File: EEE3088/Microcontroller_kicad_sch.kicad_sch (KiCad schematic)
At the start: 9 parts

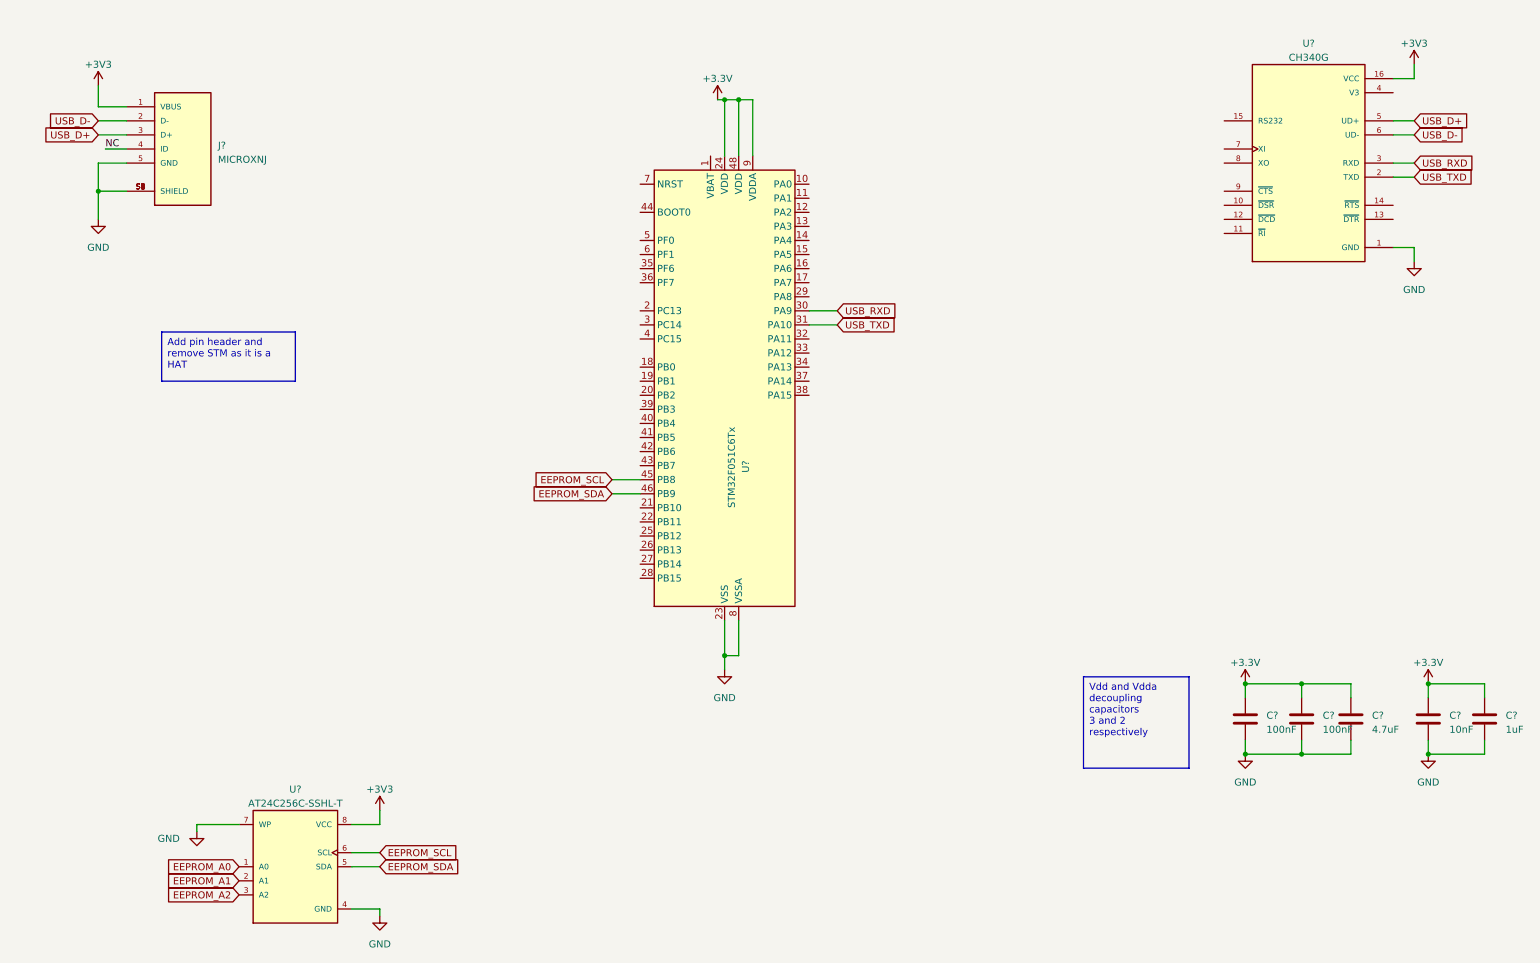
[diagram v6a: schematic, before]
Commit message: New microcontroller section
Finished and neatened up
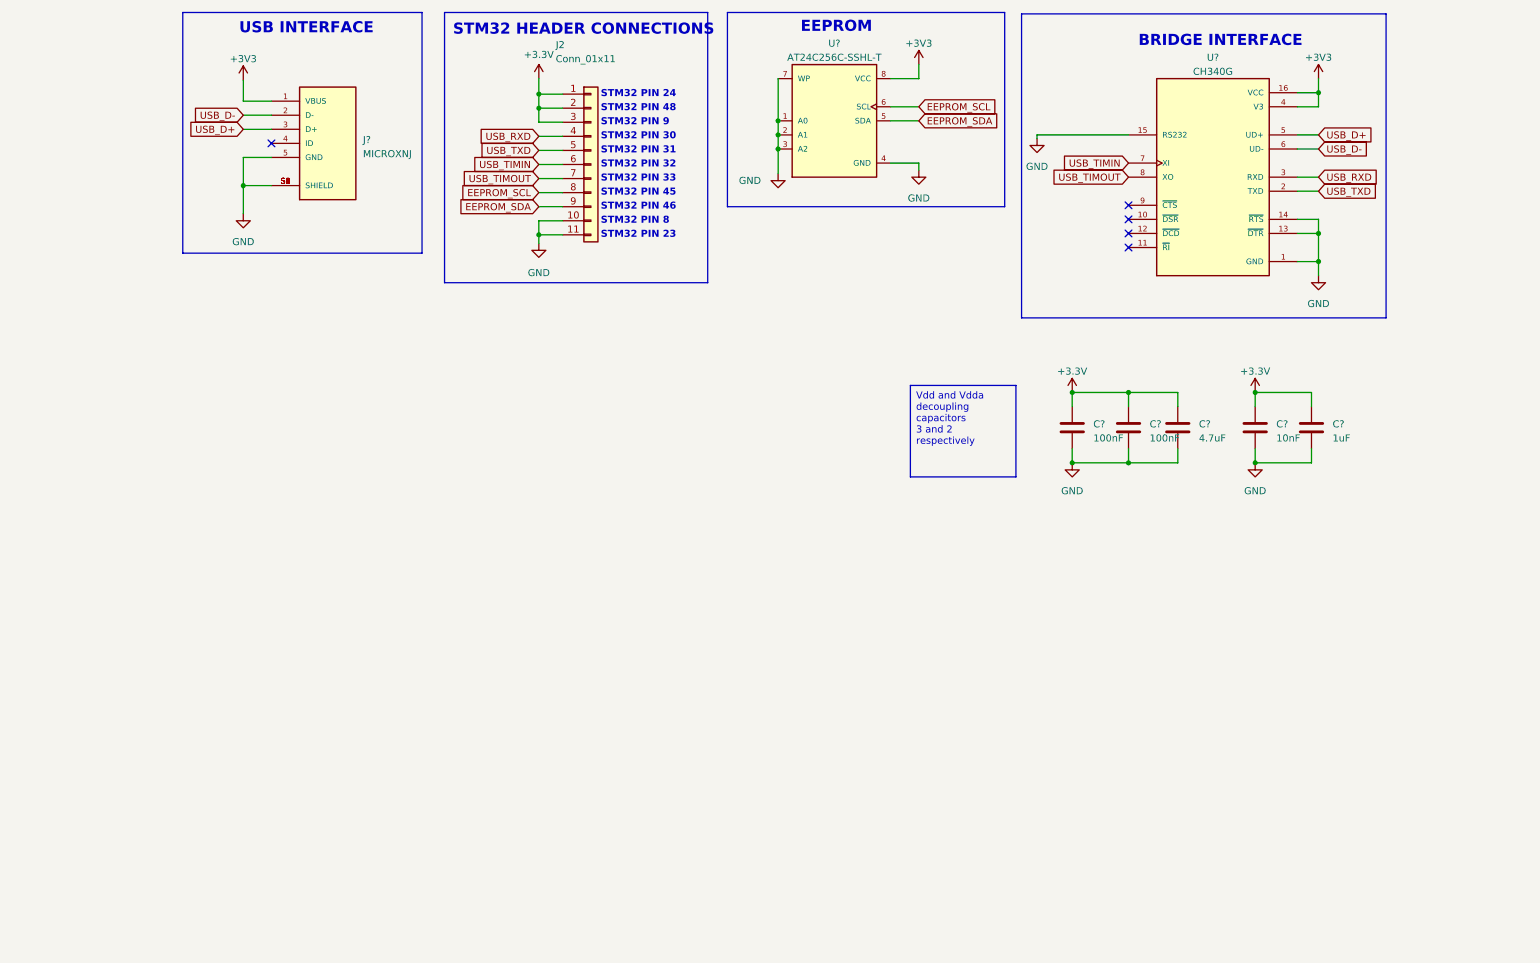
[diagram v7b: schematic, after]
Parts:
- removed U?: STM32F051C6Tx, Package_QFP:LQFP-48_7x7mm_P0.5mm, symbol MCU_ST_STM32F0:STM32F051C6Tx
- added J2: Conn_01x11, symbol Connector_Generic:Conn_01x11
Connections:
- net EEPROM_A0 is gone; now on net GND: U?.1 (A0)
- net EEPROM_A1 is gone; now on net GND: U?.2 (A1)
- net EEPROM_A2 is gone; now on net GND: U?.3 (A2)
- net +3.3V: now also J2.1 (Pin_1), J2.2 (Pin_2), J2.3 (Pin_3)
- net +3V3: now also U?.4 (V3)
- net EEPROM_SCL: now also J2.8 (Pin_8)
- net EEPROM_SDA: now also J2.9 (Pin_9)
- net GND: now also U?.13 (~{DTR}), U?.14 (~{RTS}), U?.15 (RS232), J2.10 (Pin_10), J2.11 (Pin_11)
- net USB_RXD: now also J2.4 (Pin_4)
- net USB_TXD: now also J2.5 (Pin_5)
- net USB_TIMIN: now reaches U?.7 (XI)
- net USB_TIMIN: now also J2.6 (Pin_6)
- net USB_TIMOUT: now reaches U?.8 (XO)
- net USB_TIMOUT: now also J2.7 (Pin_7)
- net NC: no longer names the net of J?.4 (ID)
- no-connect marks 0 -> 5
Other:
- note added: "BRIDGE INTERFACE"
- note added: "EEPROM"
- note added: "STM32 HEADER CONNECTIONS"
- note added: "STM32 PIN 23"
- note added: "STM32 PIN 24"
- note added: "STM32 PIN 30"
- note added: "STM32 PIN 31"
- note added: "STM32 PIN 32"
- note added: "STM32 PIN 33"
- note added: "STM32 PIN 45"
- note added: "STM32 PIN 46"
- note added: "STM32 PIN 48"
- note added: "STM32 PIN 8"
- note added: "STM32 PIN 9"
- note added: "USB INTERFACE"
- moved on the sheet: C?, J?, U?

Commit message: better microcontroller sheet
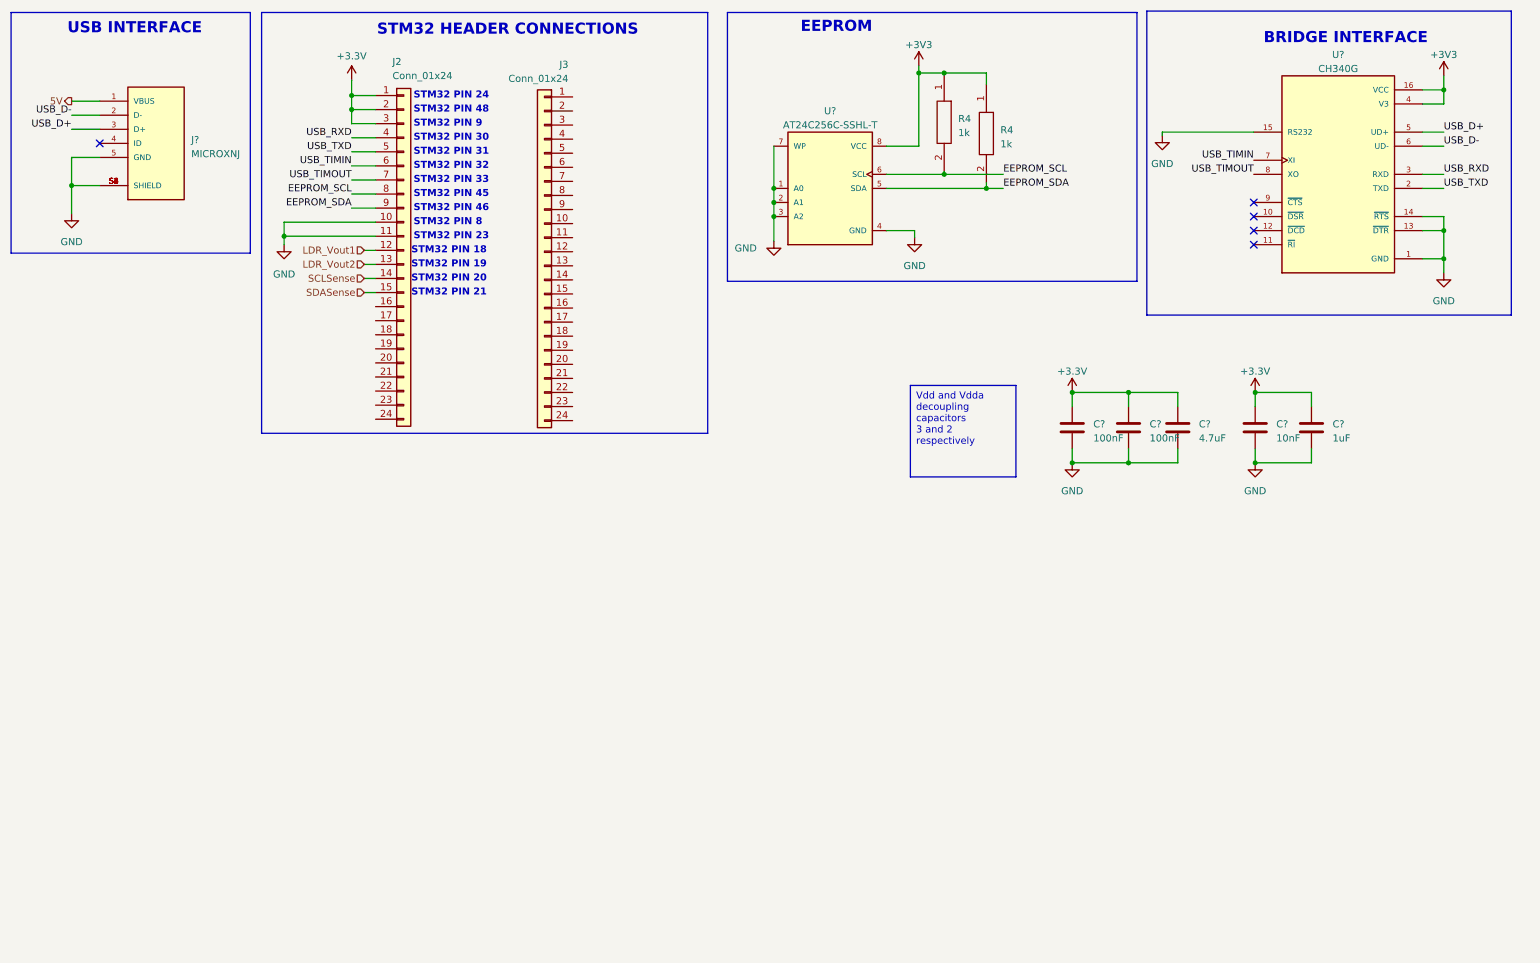
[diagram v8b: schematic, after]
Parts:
- removed J2: Conn_01x11, symbol Connector_Generic:Conn_01x11
- added J2, J3: Conn_01x24, symbol Connector_Generic:Conn_01x24
- added R4 (x2): 1k, RESC1005X40N, symbol 0402WGF1001TCE:0402WGF1001TCE
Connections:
- net +3.3V: now also J2.1 (Pin_1), J2.2 (Pin_2), J2.3 (Pin_3)
- net +3V3: now also R4.1, R4.1; no longer J?.1 (VBUS)
- net EEPROM_SCL: now also J2.8 (Pin_8), R4.2
- net EEPROM_SDA: now also J2.9 (Pin_9), R4.2
- net GND: now also J2.10 (Pin_10), J2.11 (Pin_11)
- net USB_RXD: now also J2.4 (Pin_4)
- net USB_TIMIN: now also J2.6 (Pin_6)
- net USB_TIMOUT: now also J2.7 (Pin_7)
- net USB_TXD: now also J2.5 (Pin_5)
- new net 5V: J?.1 (VBUS)
- new net LDR_Vout1: J2.12 (Pin_12)
- new net LDR_Vout2: J2.13 (Pin_13)
- new net SCLSense: J2.14 (Pin_14)
- new net SDASense: J2.15 (Pin_15)
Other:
- note added: "STM32 PIN 18"
- note added: "STM32 PIN 19"
- note added: "STM32 PIN 20"
- note added: "STM32 PIN 21"
- moved on the sheet: J?, U?
